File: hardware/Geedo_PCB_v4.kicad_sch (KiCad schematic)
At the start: 21 parts, among them J1 USB-C, J2 BATTERY, J3 OLED, SW1 MAIN_BTN, SW2 BOOT_BTN, SW3 RESET_BTN, U1 MCP73831, U2 AMS1117-3.3, U3 ESP32-C3-MINI-1

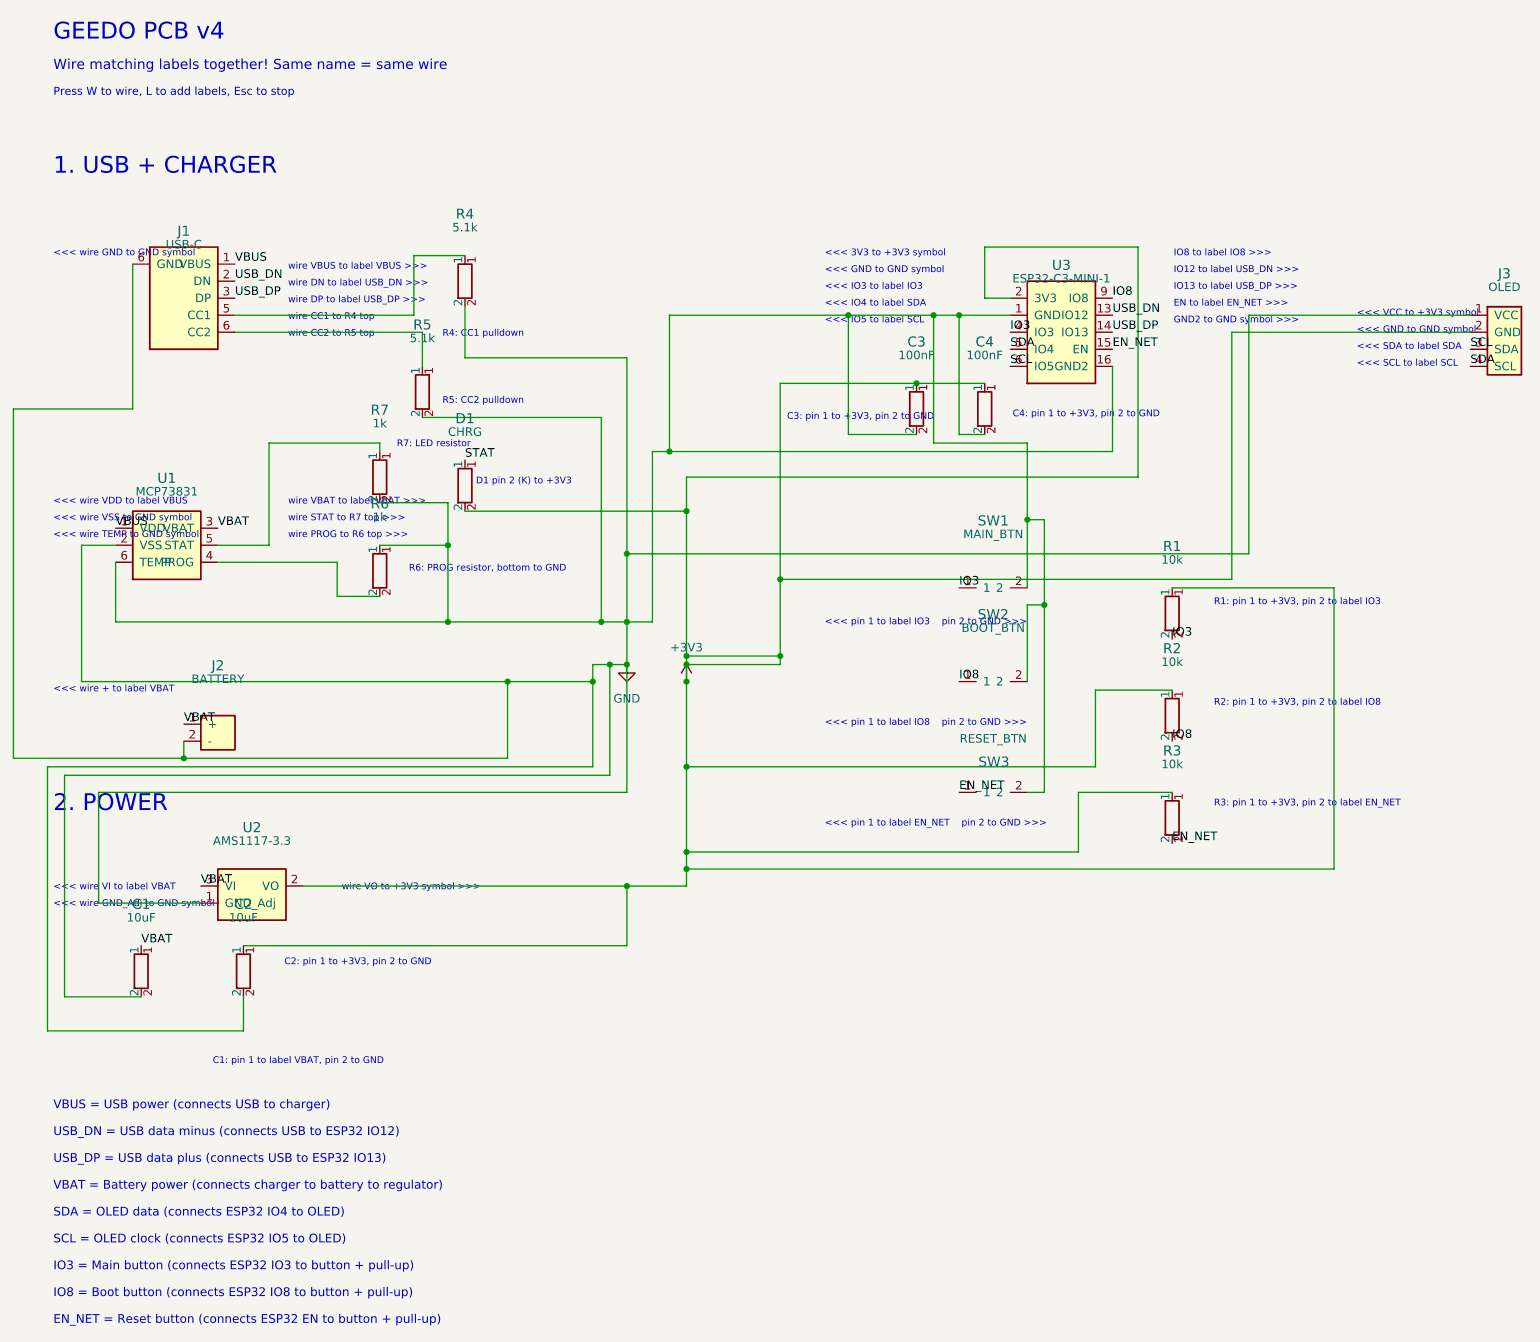
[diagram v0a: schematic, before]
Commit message: hardware: repair Geedo PCB v4 netlists (USB-C, ESP32-C3 pin map, charger)
The custom schematic symbols (ESP32C3, USBC, MCP73831) used invented pin
numbers that did not match their real footprints, leaving the USB-C
connector fully unconnected and scrambling the ESP32 module and charger
nets onto wrong physical pads. Renumbered all three symbols to the real
device pad maps, rewrote the board pad nets to match, moved the BOOT
button to IO9, added the required IO2 boot-strap pull-up (R8) and a VBUS
input cap (C5), rewired the charge-status LED chain, changed the PROG
resistor to 4.7k (~215mA), and removed 140 track segments routed to wrong
pads. Schematic/board consistency verified pad-by-pad with an independent
connectivity trace. See hardware/README.md for the full repair record and
remaining routing work.

Co-Authored-By: Claude Fable 5 <noreply@anthropic.com>
Claude-Session: https://claude.ai/code/session_011AnT632DFTLYxaJBrifUnG
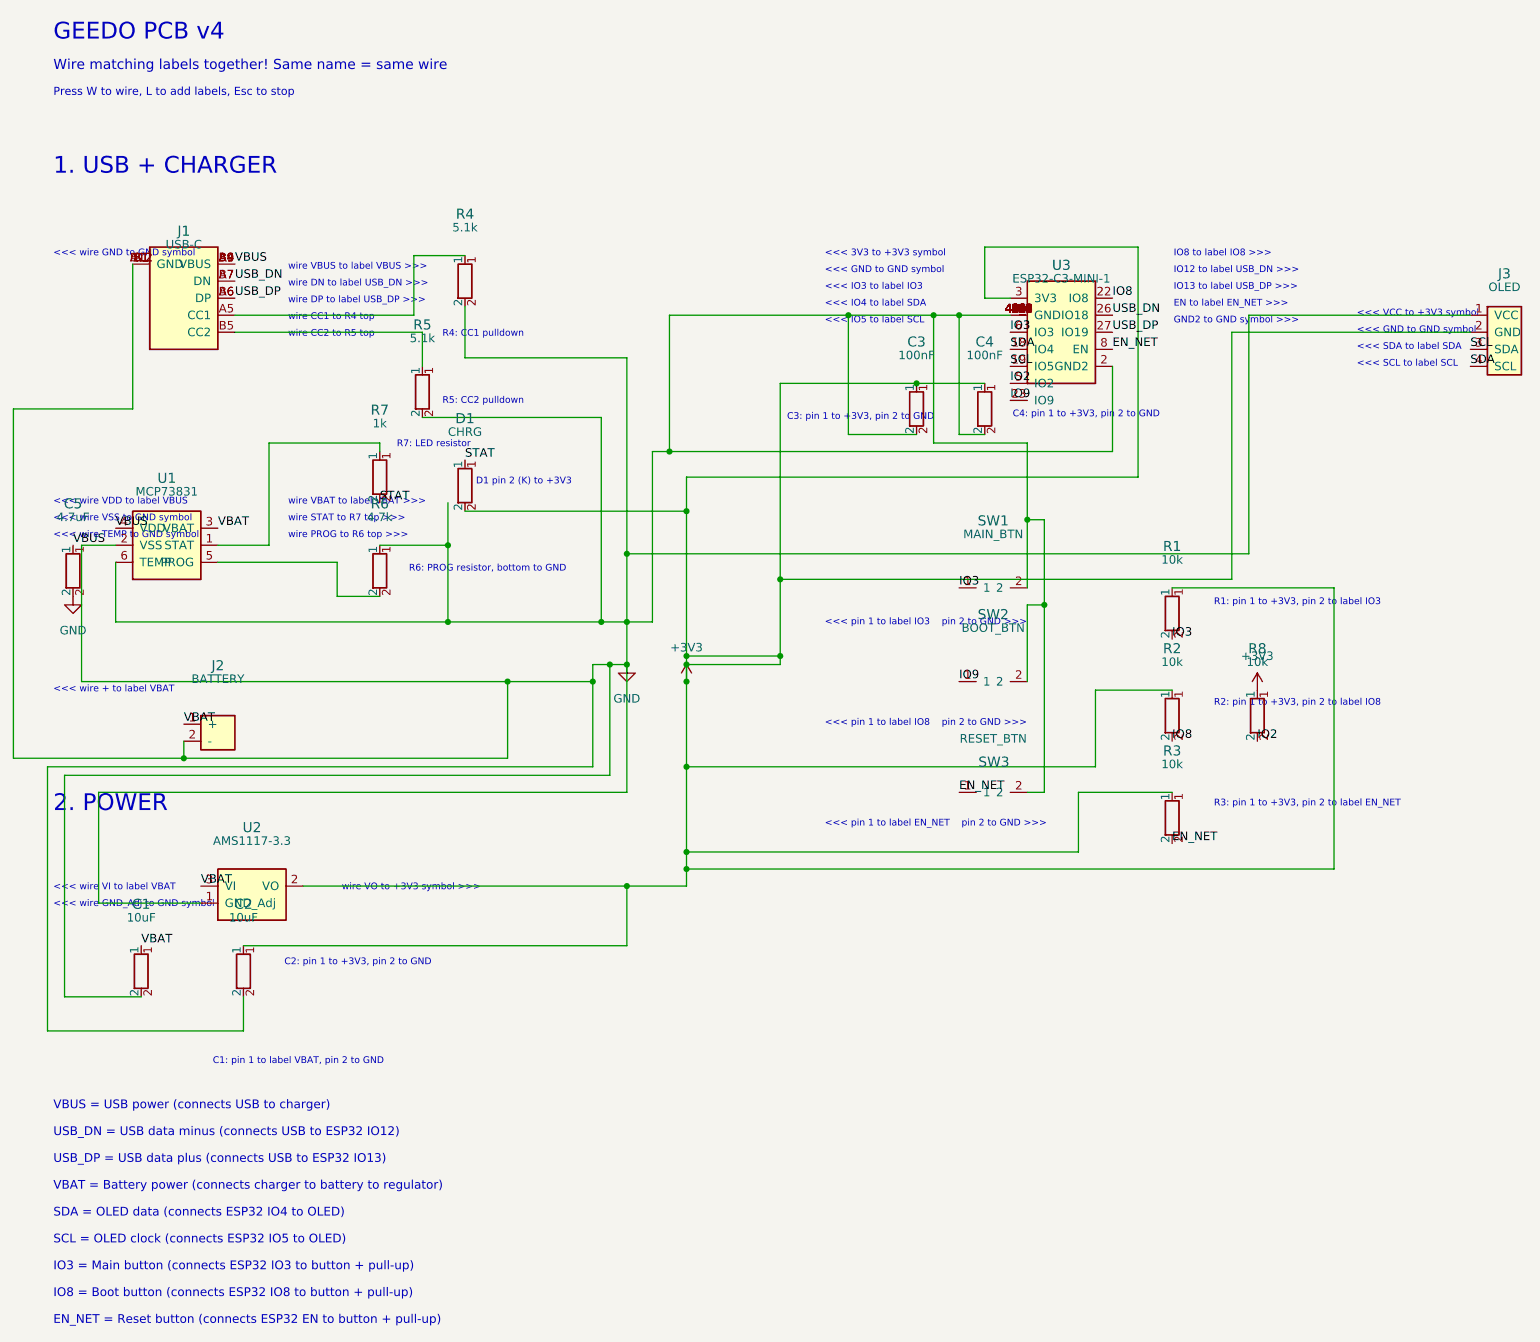
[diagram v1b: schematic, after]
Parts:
- added C5: 4.7uF, Capacitor_SMD:C_0402_1005Metric, symbol Device:C
- added R8: 10k, Resistor_SMD:R_0402_1005Metric, symbol Device:R
- R6: value 1k -> 4.7k
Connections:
- net +3V3: now also U3.3 (3V3), R8.1; no longer U3.2 (3V3)
- net EN_NET: now also U3.8 (EN); no longer U3.15 (EN)
- net GND: now also J1.A1 (GND), J1.A12 (GND), J1.B1 (GND), J1.B12 (GND), J1.S1 (GND), U3.11 (GND), U3.14 (GND), U3.2 (GND2), U3.36 (GND), U3.37 (GND), U3.38 (GND), U3.39 (GND), U3.40 (GND), U3.41 (GND), U3.42 (GND), U3.43 (GND), U3.44 (GND), U3.45 (GND), U3.46 (GND), U3.47 (GND), U3.48 (GND), U3.49_1 (GND), U3.49_2 (GND), U3.49_3 (GND), U3.49_4 (GND), U3.49_5 (GND), U3.49_6 (GND), U3.49_7 (GND), U3.49_8 (GND), U3.49_9 (GND), U3.50 (GND), U3.51 (GND), U3.52 (GND), U3.53 (GND), C5.2; no longer J1.6 (GND), R7.2, U3.16 (GND2)
- net IO3: now also U3.6 (IO3); no longer U3.4 (IO3)
- net IO8: now also U3.22 (IO8); no longer SW2.1, U3.9 (IO8)
- net SCL: now also U3.19 (IO5); no longer U3.6 (IO5)
- net SDA: now also U3.18 (IO4); no longer U3.5 (IO4)
- net STAT: now also R7.2
- net USB_DN: now also J1.A7 (DN), J1.B7 (DN), U3.26 (IO18); no longer J1.2 (DN), U3.13 (IO12)
- net USB_DP: now also J1.A6 (DP), J1.B6 (DP), U3.27 (IO19); no longer J1.3 (DP), U3.14 (IO13)
- net VBUS: now also J1.A4 (VBUS), J1.A9 (VBUS), J1.B4 (VBUS), J1.B9 (VBUS), U1.4 (VDD), C5.1; no longer J1.1 (VBUS), U1.1 (VDD)
- net at R4.1: now also J1.A5 (CC1); no longer J1.5 (CC1)
- net at R5.1: now also J1.B5 (CC2); no longer J1.6 (GND)
- net at R6.2: now also U1.5 (PROG); no longer U1.4 (PROG)
- net at R7.1: now also U1.1 (STAT); no longer U1.5 (STAT)
- new net IO2: R8.2, U3.5 (IO2)
- new net IO9: SW2.1, U3.23 (IO9)

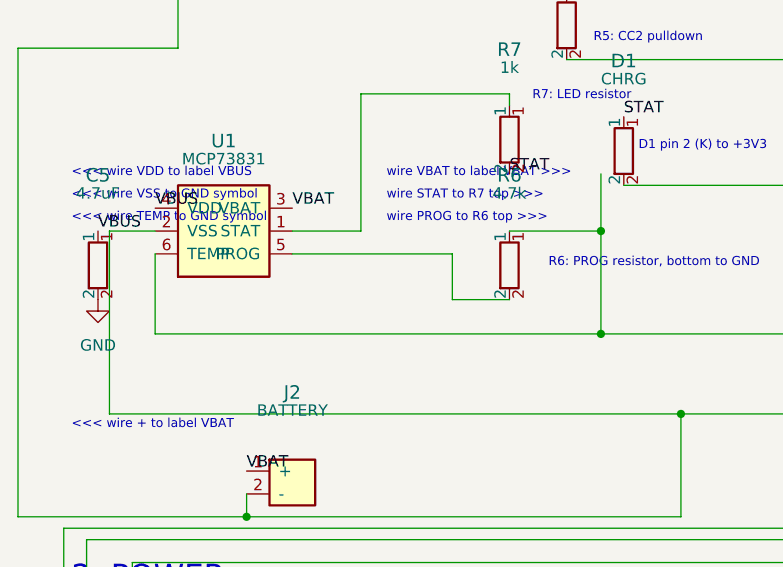
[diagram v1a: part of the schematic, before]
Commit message: hardware: drop the phantom TEMP pin from the charger symbol
The MCP73831 symbol carried a sixth pin (TEMP) that the real SOT-23-5 part
does not have, wired into the GND bus. That was the board's one remaining
schematic-parity error: no pad exists for pin 6. Removed the pin from the
library symbol and the U1 instance, plus the two wires that fed only it -
the GND bus keeps its run from x=83.82 onward, and U1's real ground (VSS,
pin 2) has its own connection.

Schematic-to-board netlist re-verified pad-by-pad: 29/29 critical nets
correct, still consistent.

Co-Authored-By: Claude Opus 5 <noreply@anthropic.com>
Claude-Session: https://claude.ai/code/session_011AnT632DFTLYxaJBrifUnG
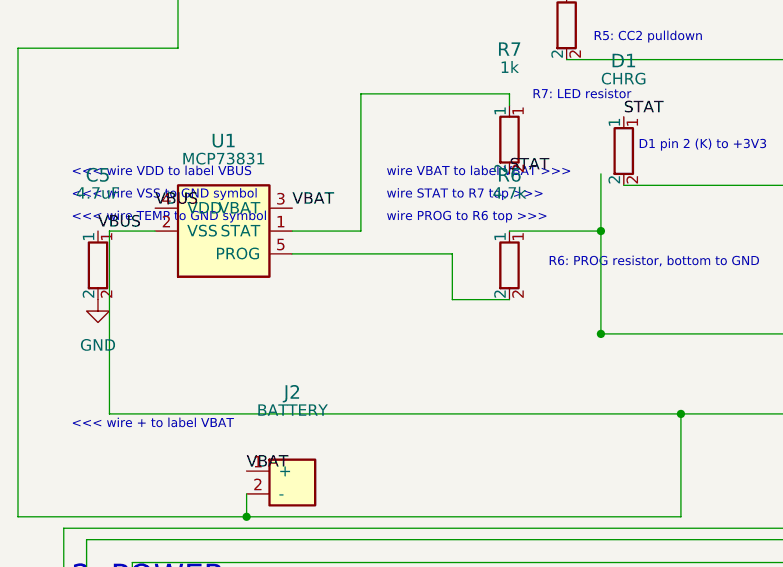
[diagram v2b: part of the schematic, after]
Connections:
- net GND: no longer U1.6 (TEMP)
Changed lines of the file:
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@@
-	(wire
-		(pts
-			(xy 34.29 102.87) (xy 83.82 102.87)
-		)
-		(stroke
-			(width 0)
-			(type default)
-		)
-	)
 	(wire
 		(pts
@@
 		(pts
 			(xy 177.8 137.16) (xy 119.38 137.16)
-		)
-		(stroke
-			(width 0)
-			(type default)
-		)
-	)
-	(wire
-		(pts
-			(xy 34.29 93.98) (xy 34.29 102.87)
 		)
 		(stroke
@@
 		(pin "1"
 		)
-		(pin "6"
-		)
 		(instances

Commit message: hardware: replace AMS1117 with MCP1826S low-dropout regulator
The AMS1117 needs ~1.1 V of headroom, so on a LiPo it only holds 3.3 V near
full charge: at 3.7 V nominal the rail sits around 3.0 V, and an ESP32-C3's
300-400 mA WiFi transmit bursts widen the dropout further. The board would
have reset during WiFi at half battery - fatal for a robot that depends on
WiFi for updates and events.

MCP1826S-3302 drops 0.25 V and holds 3.3 V down to ~3.55 V of battery, using
the same SOT-223 footprint. It is not pin-compatible (AMS1117 is GND/Vout/Vin
with the tab on Vout; MCP1826S is Vin/GND/Vout with the tab on GND), so U2's
pads were remapped and VBAT/3V3 re-routed around it. The schematic symbol was
renumbered rather than redrawn, leaving every existing wire in place. The tab
now bonds to the ground pour, which also helps thermally.

Added C6, 1 uF on the back 2 mm from the output pin, as a local output
capacitor - C2's 10 uF sits 9 mm away. Its first position overlapped a 3V3
track and a VBAT via; the clearance audit caught both and it was moved to a
spot verified clear of every pad, track and via, with a gap even to same-net
pads.

Verified: schematic-to-board netlist 29/29 correct, every net except the
unfilled GND pour resolves to one island, and clearance is unchanged at the
9 pre-existing violations with none introduced.

Co-Authored-By: Claude Opus 5 <noreply@anthropic.com>
Claude-Session: https://claude.ai/code/session_011AnT632DFTLYxaJBrifUnG
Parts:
- added C6: 1uF, Capacitor_SMD:C_0402_1005Metric, symbol Device:C
- U2: value AMS1117-3.3 -> MCP1826S-3302; symbol Geedo:AMS1117 -> Geedo:MCP1826S
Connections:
- net +3V3: now also U2.3 (VO), C6.1; no longer U2.2 (VO)
- net GND: now also U2.2 (GND), C6.2; no longer U2.1 (GND_Adj)
- net VBAT: now also U2.1 (VI); no longer U2.3 (VI)
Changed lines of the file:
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@@
+	(symbol
+		(lib_id "power:+3V3")
+		(at 68.58 151.13 0)
+		(unit 1)
+		(exclude_from_sim no)
+		(in_bom yes)
+		(on_board yes)
+		(dnp no)
+		(fields_autoplaced yes)
+		(property "Reference" "#PWR5"
+			(at 68.58 154.94 0)
+			(effects
+				(font
+					(size 1.27 1.27)
+				)
+				(hide yes)
+			)
+		)
+		(property "Value" "+3V3"
+			(at 68.58 146.05 0)
+			(effects
+				(font
+					(size 1.27 1.27)
+				)
+			)
+		)
+		(property "Footprint" ""
+			(at 68.58 151.13 0)
+			(effects
+				(font
+					(size 1.27 1.27)
+				)
+				(hide yes)
+			)
+		)
+		(property "Datasheet" ""
+			(at 68.58 151.13 0)
+			(effects
+				(font
+					(size 1.27 1.27)
+				)
+				(hide yes)
+			)
+		)
+		(property "Description" "Power symbol creates a global label with name \"+3V3\""
+			(at 68.58 151.13 0)
+			(effects
+				(font
+					(size 1.27 1.27)
+				)
+				(hide yes)
+			)
+		)
+		(pin "1"
+		)
+		(instances
+			(project ""
+				(path "/c1b30509-5759-4de0-8051-e295a09caa78"
+					(reference "#PWR5")
+					(unit 1)
+				)
+			)
+		)
+	)
 	(symbol
 		(lib_id "power:+3V3")
@@
 	(symbol
 		(lib_id "Device:C")
+		(at 68.58 154.94 0)
+		(unit 1)
+		(exclude_from_sim no)
+		(in_bom yes)
+		(on_board yes)
+		(dnp no)
+		(property "Reference" "C6"
+			(at 68.58 144.94 0)
+			(effects
+				(font
+					(size 1.5 1.5)
+				)
+			)
+		)
+		(property "Value" "1uF"
+			(at 68.58 146.94 0)
+			(effects
+				(font
+					(size 1.27 1.27)
+				)
+			)
+		)
+		(property "Footprint" "Capacitor_SMD:C_0402_1005Metric"
+			(at 68.58 154.94 0)
+			(effects
+				(font
+					(size 1.27 1.27)
+				)
+				(hide yes)
+			)
+		)
+		(property "Datasheet" ""
+			(at 68.58 154.94 0)
+			(effects
+				(font
+					(size 1.27 1.27)
+				)
+				(hide yes)
+			)
+		)
+		(property "Description" ""
+			(at 68.58 154.94 0)
+			(effects
+				(font
+					(size 1.27 1.27)
+				)
+				(hide yes)
+			)
+		)
+		(pin "1"
+		)
+		(pin "2"
+		)
+		(instances
+			(project "Geedo_PCB_v4"
+				(path "/c1b30509-5759-4de0-8051-e295a09caa78"
+					(reference "C6")
+					(unit 1)
+				)
+			)
+		)
+	)
+	(symbol
+		(lib_id "Device:C")
 		(at 27.94 95.25 0)
 		(unit 1)
@@
 	)
 	(symbol
-		(lib_id "Geedo:AMS1117")
+		(lib_id "Geedo:MCP1826S")
 		(at 54.61 143.51 0)
 		(unit 1)
@@
 			)
 		)
-		(property "Value" "AMS1117-3.3"
+		(property "Value" "MCP1826S-3302"
 			(at 54.61 135.51 0)
 			(effects
@@
 					(unit 1)
 				)
+			)
+		)
+	)
+	(symbol
+		(lib_name "GND_1")
+		(lib_id "power:GND")
+		(at 68.58 158.75 0)
+		(unit 1)
+		(exclude_from_sim no)
+		(in_bom yes)
+		(on_board yes)
+		(dnp no)
+		(fields_autoplaced yes)
+		(property "Reference" "#PWR6"
+			(at 68.58 165.1 0)
+			(effects
+				(font
+					(size 1.27 1.27)
+				)
+				(hide yes)
+			)
+		)
+		(property "Value" "GND"
+			(at 68.58 163.83 0)
+			(effects
+				(font
+					(size 1.27 1.27)
+				)
+			)
+		)
+		(property "Footprint" ""
+			(at 68.58 158.75 0)
+			(effects
+				(font
+					(size 1.27 1.27)
+				)
+				(hide yes)
+			)
+		)
+		(property "Datasheet" ""
+			(at 68.58 158.75 0)
+			(effects
+				(font
+					(size 1.27 1.27)
+				)
+				(hide yes)
+			)
+		)
+		(property "Description" "Power symbol creates a global label with name \"GND\" , ground"
+			(at 68.58 158.75 0)
+			(effects
+				(font
+					(size 1.27 1.27)
+				)
+				(hide yes)
+			)
+		)
+		(pin "1"
+		)
+		(instances
+			(project ""
+				(path "/c1b30509-5759-4de0-8051-e295a09caa78"
+					(reference "#PWR6")
+					(unit 1)
+				)

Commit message: hardware: add C7, the EN power-on reset capacitor
1 uF from EN to ground on the back, directly under the module's EN pad, 0.55 mm
from it. With R3's 10 k pull-up this forms the RC delay Espressif's design
guidelines call for: reset is held low while the 3.3 V rail rises, so the chip
starts cleanly on a slow power-up instead of occasionally hanging until the
reset button is pressed.

Two placement attempts were reverted before this one, both caught by the
verifiers rather than reaching the board:

- The first put the schematic symbol at coordinates crossed by the +3V3 bus
  wire at y=151.13, which merged EN into +3V3. The symbol now sits in space
  checked clear of every wire, symbol, label and junction.
- The second assumed pad 1 was the left-hand pad. The 0402 footprint is placed
  at rot 180, so pad 1 is on the right - meaning the ground pad landed where
  the EN pad was meant to go, shorting EN to ground and holding the chip in
  permanent reset. Placement is now computed from the footprint's real pad
  offsets and rotation, and tried at both orientations.

Verified after placing and again after routing: schematic-to-board netlist
29/29 correct, EN carries exactly U3.8, R3.2, SW3.1 and C7.1, and clearance is
unchanged at the 9 pre-existing violations with none introduced.

Co-Authored-By: Claude Opus 5 <noreply@anthropic.com>
Claude-Session: https://claude.ai/code/session_011AnT632DFTLYxaJBrifUnG
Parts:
- added C7: 1uF, Capacitor_SMD:C_0402_1005Metric, symbol Device:C
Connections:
- net EN_NET: now also C7.1
- net GND: now also C7.2
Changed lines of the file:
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@@
+	)
+	(label "EN_NET"
+		(at 113.82 56.19 0)
+		(effects
+			(font
+				(size 1.27 1.27)
+			)
+			(justify left bottom)
+		)
 	)
 	(label "EN_NET"
@@
 	(symbol
 		(lib_id "Device:C")
+		(at 113.82 60.0 0)
+		(unit 1)
+		(exclude_from_sim no)
+		(in_bom yes)
+		(on_board yes)
+		(dnp no)
+		(property "Reference" "C7"
+			(at 113.82 50.0 0)
+			(effects
+				(font
+					(size 1.5 1.5)
+				)
+			)
+		)
+		(property "Value" "1uF"
+			(at 113.82 52.0 0)
+			(effects
+				(font
+					(size 1.27 1.27)
+				)
+			)
+		)
+		(property "Footprint" "Capacitor_SMD:C_0402_1005Metric"
+			(at 113.82 60.0 0)
+			(effects
+				(font
+					(size 1.27 1.27)
+				)
+				(hide yes)
+			)
+		)
+		(property "Datasheet" ""
+			(at 113.82 60.0 0)
+			(effects
+				(font
+					(size 1.27 1.27)
+				)
+				(hide yes)
+			)
+		)
+		(property "Description" ""
+			(at 113.82 60.0 0)
+			(effects
+				(font
+					(size 1.27 1.27)
+				)
+				(hide yes)
+			)
+		)
+		(pin "1"
+		)
+		(pin "2"
+		)
+		(instances
+			(project "Geedo_PCB_v4"
+				(path "/c1b30509-5759-4de0-8051-e295a09caa78"
+					(reference "C7")
+					(unit 1)
+				)
+			)
+		)
+	)
+	(symbol
+		(lib_id "Device:C")
 		(at 68.58 154.94 0)
 		(unit 1)
@@
 					(unit 1)
 				)
+			)
+		)
+	)
+	(symbol
+		(lib_name "GND_1")
+		(lib_id "power:GND")
+		(at 113.82 63.81 0)
+		(unit 1)
+		(exclude_from_sim no)
+		(in_bom yes)
+		(on_board yes)
+		(dnp no)
+		(fields_autoplaced yes)
+		(property "Reference" "#PWR7"
+			(at 113.82 70.16 0)
+			(effects
+				(font
+					(size 1.27 1.27)
+				)
+				(hide yes)
+			)
+		)
+		(property "Value" "GND"
+			(at 113.82 68.89 0)
+			(effects
+				(font
+					(size 1.27 1.27)
+				)
+			)
+		)
+		(property "Footprint" ""
+			(at 113.82 63.81 0)
+			(effects
+				(font
+					(size 1.27 1.27)
+				)
+				(hide yes)
+			)
+		)
+		(property "Datasheet" ""
+			(at 113.82 63.81 0)
+			(effects
+				(font
+					(size 1.27 1.27)
+				)
+				(hide yes)
+			)
+		)
+		(property "Description" "Power symbol creates a global label with name \"GND\" , ground"
+			(at 113.82 63.81 0)
+			(effects
+				(font
+					(size 1.27 1.27)
+				)
+				(hide yes)
+			)
+		)
+		(pin "1"
+		)
+		(instances
+			(project ""
+				(path "/c1b30509-5759-4de0-8051-e295a09caa78"
+					(reference "#PWR7")
+					(unit 1)
+				)
